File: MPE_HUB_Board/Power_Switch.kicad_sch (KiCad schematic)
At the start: 9 parts, among them U5 VND7050AJTR

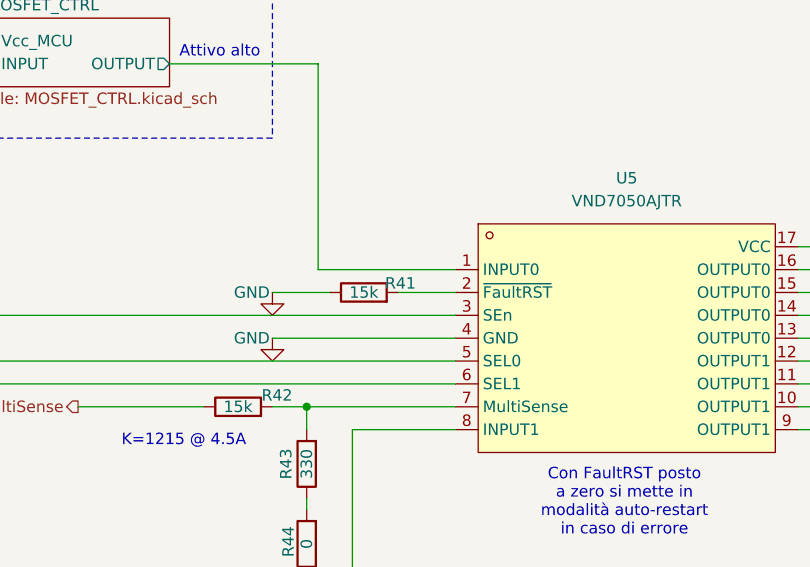
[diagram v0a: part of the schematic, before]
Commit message: Risolto problema reset (Nel firmware V2)
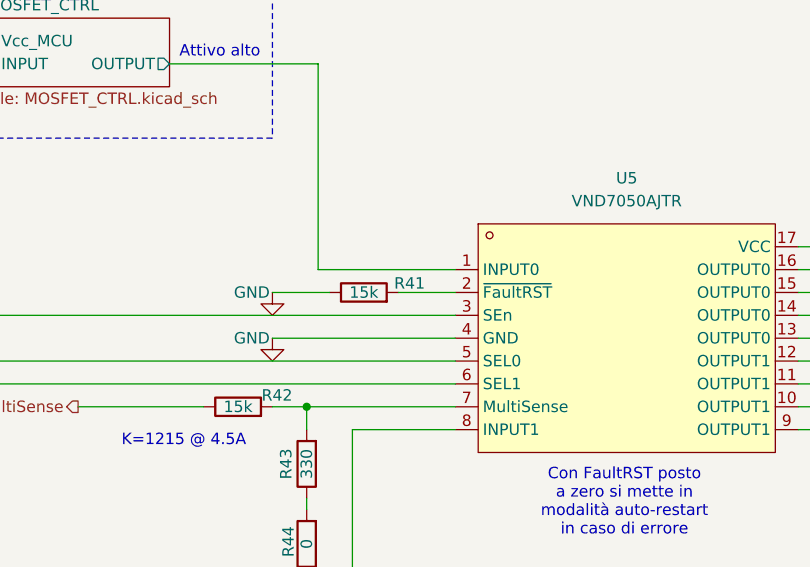
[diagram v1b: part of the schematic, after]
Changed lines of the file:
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@@
 	(generator_version "9.0")
 	(paper "A4")
+	(title_block
+		(date "2025-03-21")
+	)
 	(rectangle
 		(start 229.235 144.145)
@@
 		(dnp no)
 		(property "Reference" "R41"
-			(at 175.514 58.674 90)
-			(effects
-				(font
+			(at 176.53 58.674 90)
+			(effects
+				(font

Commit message: Update 04/07/2025
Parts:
- added R87: 15k, Resistor_SMD:R_0603_1608Metric, symbol Device:R
- R43: value 330 -> 1K; LCSC C23138 -> C21190; LCSC Part (none) -> C21190
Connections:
- net MOSFET_CTRL/OUTPUT is gone; now on net EC_0: U5.1 (INPUT0)
- net MOSFET_CTRL2/OUTPUT is gone; now on net SEL_0: U5.5 (SEL0)
- net MOSFET_CTRL3/OUTPUT is gone; now on net SEL_1: U5.6 (SEL1)
- net MOSFET_CTRL4/OUTPUT is gone; now on net EC_1: U5.8 (INPUT1)
- net Vcc_MCU: now also R87.1
- net MOSFET_CTRL1/OUTPUT: no longer names the net of U5.3 (SEn)
- net MOSFET_CTRL1/OUTPUT: now also R87.2
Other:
- removed sheet MOSFET_CTRL
- removed sheet MOSFET_CTRL1
- removed sheet MOSFET_CTRL2
- removed sheet MOSFET_CTRL3
- removed sheet MOSFET_CTRL4
- note added: "GPIO ACTIVE HIGH"
- note removed: "Attivo alto"
- moved on the sheet: R41, R42, R44, U5

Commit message: Update 08/07/2025
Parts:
- added C38: 100nf, Capacitor_SMD:C_0603_1608Metric, symbol easyeda2kicad:CC0603KRX7R9BB104
- added R100, R98: 15k, Resistor_SMD:R_0603_1608Metric, symbol Device:R
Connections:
- net GND: now also C38.1, R100.1
- net MultiSense: now also C38.2, R98.2
- new net: R100.2, R98.1
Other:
- moved on the sheet: R41, R42, R43, R44, R87, U5

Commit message: HUB Hardware V1.1.0
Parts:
- removed C38: 100nf, Capacitor_SMD:C_0603_1608Metric, symbol easyeda2kicad:CC0603KRX7R9BB104
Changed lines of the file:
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@@
-	)
-	(rectangle
-		(start 87.63 100.965)
-		(end 100.33 132.08)
-		(stroke
-			(width 0)
-			(type dot)
-			(color 0 132 0 1)
-		)
-		(fill
-			(type none)
-		)
 	)
 	(rectangle
@@
 		(at 102.235 127 0)
 		(size 13.97 5.08)
-		(margins 0.9525 0.9525 0.9525 0.9525)
-		(stroke
-			(width 0)
-			(type solid)
-			(color 0 132 0 1)
-		)
-		(fill
-			(type none)
-		)
-		(effects
-			(font
-				(size 1.27 1.27)
-				(color 0 132 0 1)
-			)
-		)
-	)
-	(text_box "EXTERNAL CAP"
-		(exclude_from_sim no)
-		(at 87.63 127 0)
-		(size 12.7 5.08)
 		(margins 0.9525 0.9525 0.9525 0.9525)
 		(stroke
@@
 	)
 	(junction
-		(at 93.98 88.9)
-		(diameter 0)
-		(color 0 0 0 0)
-	)
-	(junction
 		(at 194.31 78.74)
 		(diameter 0)
@@
 	(wire
 		(pts
-			(xy 93.98 115.57) (xy 93.98 120.65)
-		)
-		(stroke
-			(width 0)
-			(type default)
-		)
-	)
-	(wire
-		(pts
 			(xy 137.16 119.38) (xy 137.16 120.65)
 		)
@@
 	(wire
 		(pts
-			(xy 74.93 88.9) (xy 93.98 88.9)
-		)
-		(stroke
-			(width 0)
-			(type default)
-		)
-	)
-	(wire
-		(pts
-			(xy 93.98 88.9) (xy 93.98 105.41)
-		)
-		(stroke
-			(width 0)
-			(type default)
-		)
-	)
-	(wire
-		(pts
 			(xy 271.78 133.35) (xy 279.4 133.35)
 		)
@@
 	(wire
 		(pts
-			(xy 93.98 88.9) (xy 109.22 88.9)
+			(xy 100.33 88.9) (xy 109.22 88.9)
 		)
 		(stroke
@@
 	(hierarchical_label "MultiSense"
 		(shape output)
-		(at 74.93 88.9 180)
+		(at 100.33 88.9 180)
 		(effects
 			(font
@@
 				(path "/6490f62d-7c0a-4455-8633-837f094f0a1c/36a1afe1-9d7e-4453-8bd5-557c8a4303ef"
 					(reference "#PWR051")
-					(unit 1)
-				)
-			)
-		)
-	)
-	(symbol
-		(lib_name "CC0603KRX7R9BB104_2")
-		(lib_id "easyeda2kicad:CC0603KRX7R9BB104")
-		(at 93.98 110.49 90)
-		(unit 1)
-		(exclude_from_sim no)
-		(in_bom yes)
-		(on_board yes)
-		(dnp no)
-		(property "Reference" "C38"
-			(at 95.504 105.156 0)
-			(effects
-				(font
-					(size 1.27 1.27)
-				)
-				(justify right)
-			)
-		)
-		(property "Value" "100nf"
-			(at 91.186 103.632 0)
-			(effects
-				(font
-					(size 1.27 1.27)
-				)
-				(justify right)
-			)
-		)
-		(property "Footprint" "Capacitor_SMD:C_0603_1608Metric"
-			(at 101.6 110.49 0)
-			(effects
-				(font
-					(size 1.27 1.27)
-				)
-				(hide yes)
-			)
-		)
-		(property "Datasheet" "https://lcsc.com/product-detail/Multilayer-Ceramic-Capacitors-MLCC-SMD-SMT_100nF-104-10-50V_C14663.html"
-			(at 104.14 110.49 0)
-			(effects
-				(font
-					(size 1.27 1.27)
-				)
-				(hide yes)
-			)
-		)
-		(property "Description" ""
-			(at 93.98 110.49 0)
-			(effects
-				(font
-					(size 1.27 1.27)
-				)
-				(hide yes)
-			)
-		)
-		(property "LCSC Part" "C14663"
-			(at 106.68 110.49 0)
-			(effects
-				(font
-					(size 1.27 1.27)
-				)
-				(hide yes)
-			)
-		)
-		(property "LCSC" "C14663"
-			(at 95.885 107.95 0)
-			(effects
-				(font
-					(size 1.27 1.27)
-				)
-				(hide yes)
-			)
-		)
-		(pin "1"
-		)
-		(pin "2"
-		)
-		(instances
-			(project "HUB_MPE"
-				(path "/6490f62d-7c0a-4455-8633-837f094f0a1c/26b9dfe9-c957-43ca-ba2b-36e349e2ebb9"
-					(reference "C39")
-					(unit 1)
-				)
-				(path "/6490f62d-7c0a-4455-8633-837f094f0a1c/36a1afe1-9d7e-4453-8bd5-557c8a4303ef"
-					(reference "C38")
 					(unit 1)
 				)
@@
 					(unit 1)
 				)
-			)
-		)
-	)
-	(symbol
-		(lib_id "power:GND")
-		(at 93.98 120.65 0)
-		(unit 1)
-		(exclude_from_sim no)
-		(in_bom yes)
-		(on_board yes)
-		(dnp no)
-		(property "Reference" "#PWR083"
-			(at 93.98 127 0)
-			(effects
-				(font
-					(size 1.27 1.27)
-				)
-				(hide yes)
-			)
-		)
-		(property "Value" "GND"
-			(at 93.98 124.46 0)
-			(effects
-				(font
-					(size 1.27 1.27)
-				)
-			)
-		)
-		(property "Footprint" ""
-			(at 93.98 120.65 0)
-			(effects
-				(font
-					(size 1.27 1.27)
-				)
-				(hide yes)
-			)
-		)
-		(property "Datasheet" ""
-			(at 93.98 120.65 0)
-			(effects
-				(font
-					(size 1.27 1.27)
-				)
-				(hide yes)
-			)
-		)
-		(property "Description" "Power symbol creates a global label with name \"GND\" , ground"
-			(at 93.98 120.65 0)
-			(effects
-				(font
-					(size 1.27 1.27)
-				)
-				(hide yes)
-			)
-		)
-		(pin "1"
-		)
-		(instances
-			(project "HUB_MPE"
-				(path "/6490f62d-7c0a-4455-8633-837f094f0a1c/26b9dfe9-c957-43ca-ba2b-36e349e2ebb9"
-					(reference "#PWR084")
-					(unit 1)
-				)
-				(path "/6490f62d-7c0a-4455-8633-837f094f0a1c/36a1afe1-9d7e-4453-8bd5-557c8a4303ef"
-					(reference "#PWR083")
-					(unit 1)
-				)
